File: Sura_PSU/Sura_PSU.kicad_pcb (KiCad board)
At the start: 2 copper layers, 100 x 183 mm, 16 parts, among them J1 12VDC In, J2 X11, J3 X11, U1 PSU2-5, U2 NKE1212SC

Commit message: Initial commit (to be tested)
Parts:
- J1: value 12VDC In -> 12V In; footprint Connector_JST:JST_VH_B2P-VH_1x02_P3.96mm_Vertical -> Clueless_Engineer:694106301002
- moved H4 179.3 mm to (58.1, 47.7)
- moved H3 137.3 mm to (133.1, 47.7)
- moved J1 128.4 mm to (52.1, 181.7)
- moved F1 116.9 mm to (76.2, 181.7), turned to 90 degrees
- moved C1 81.8 mm to (124.4, 165.7)
- moved C2 81.8 mm to (115.5, 165.7)
- moved U1 80.3 mm to (88.9, 161.9), turned to -90 degrees
- moved C4 6.40 mm to (115.5, 112.3), turned to 90 degrees
- moved C3 6.39 mm to (106.8, 112.3), turned to 90 degrees
- moved H1 1.00 mm to (133.1, 220.7)
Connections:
- F1 pad 1: Net-(J1-Pin_2) -> Net-(F1-Pad1)
- J1 pad 1: /GND -> Net-(F1-Pad1)
- J1 pad 2: Net-(J1-Pin_2) -> /GND
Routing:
- net /GND: track 346.1 -> 285.7 mm
- net Net-(F1-Pad1): track 0.00 -> 29.1 mm
- net Net-(J1-Pin_2): track 18.5 -> 0.00 mm
- net /+12V: track 212.9 -> 224.3 mm
- net /+5V: track 152.8 -> 157.4 mm
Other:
- board text added: "Brett Hallen May 2026"
- board text added: "Regulated +12VDC Input"
- board text removed: "Brett Hallen, May 2026"
- board text removed: "WORK IN PROGRESS"

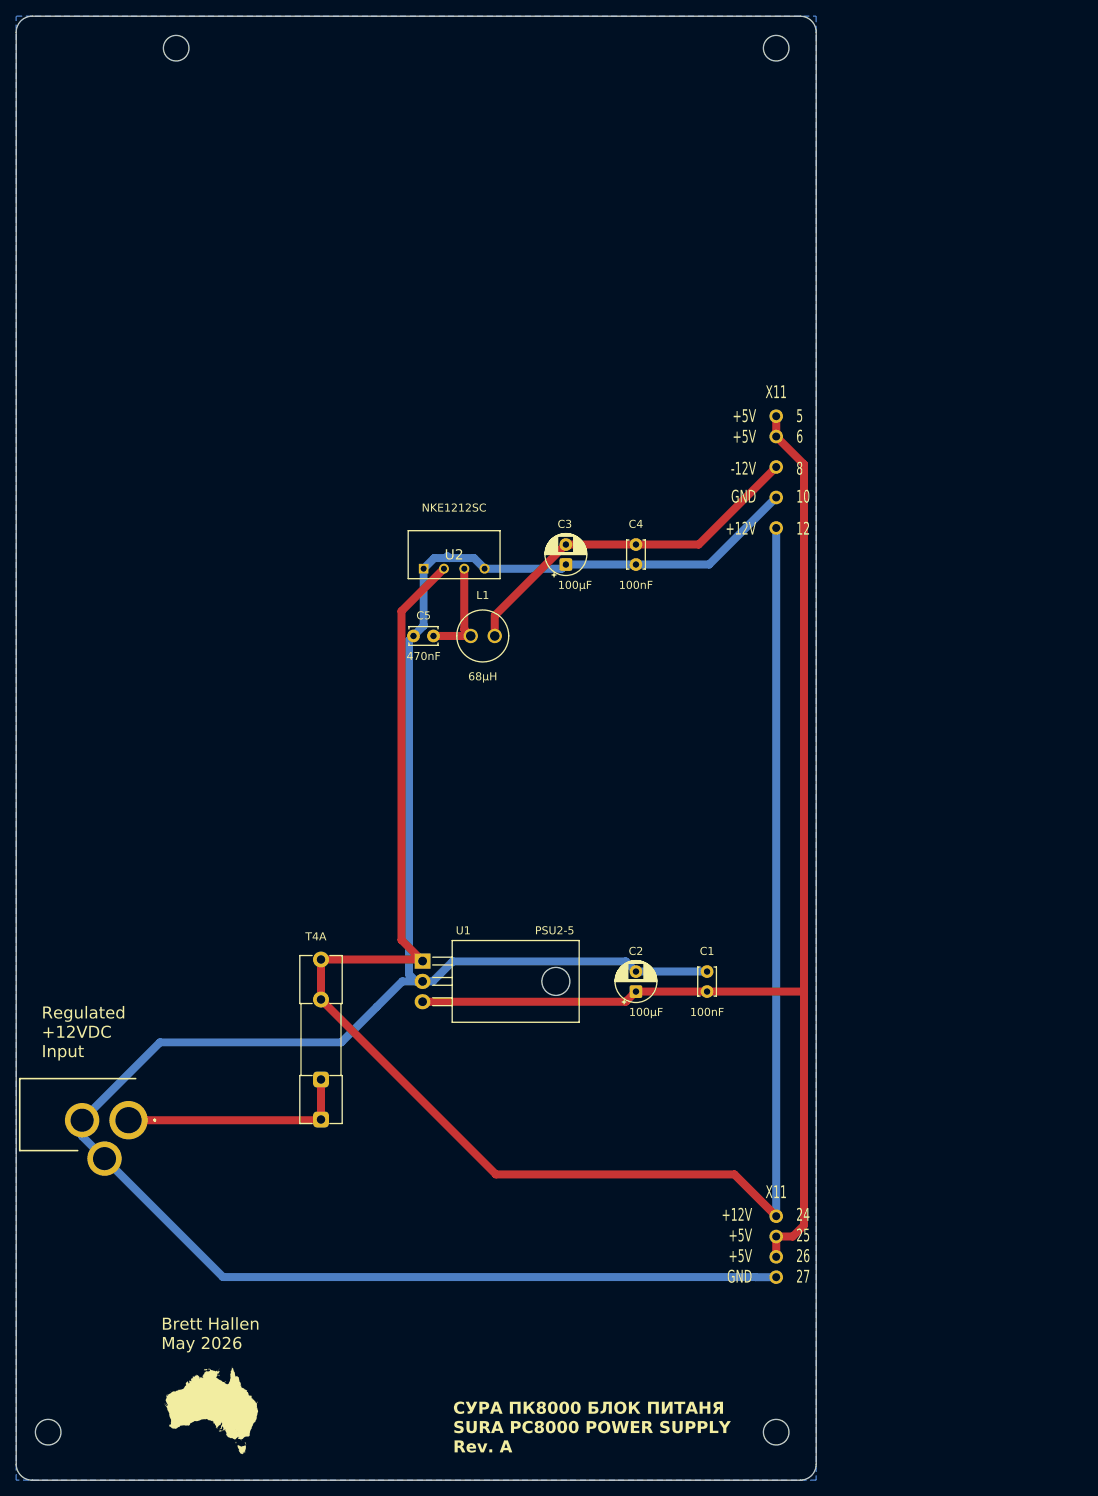
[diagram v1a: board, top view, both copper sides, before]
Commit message: Updated design (swapped 5V regulator)
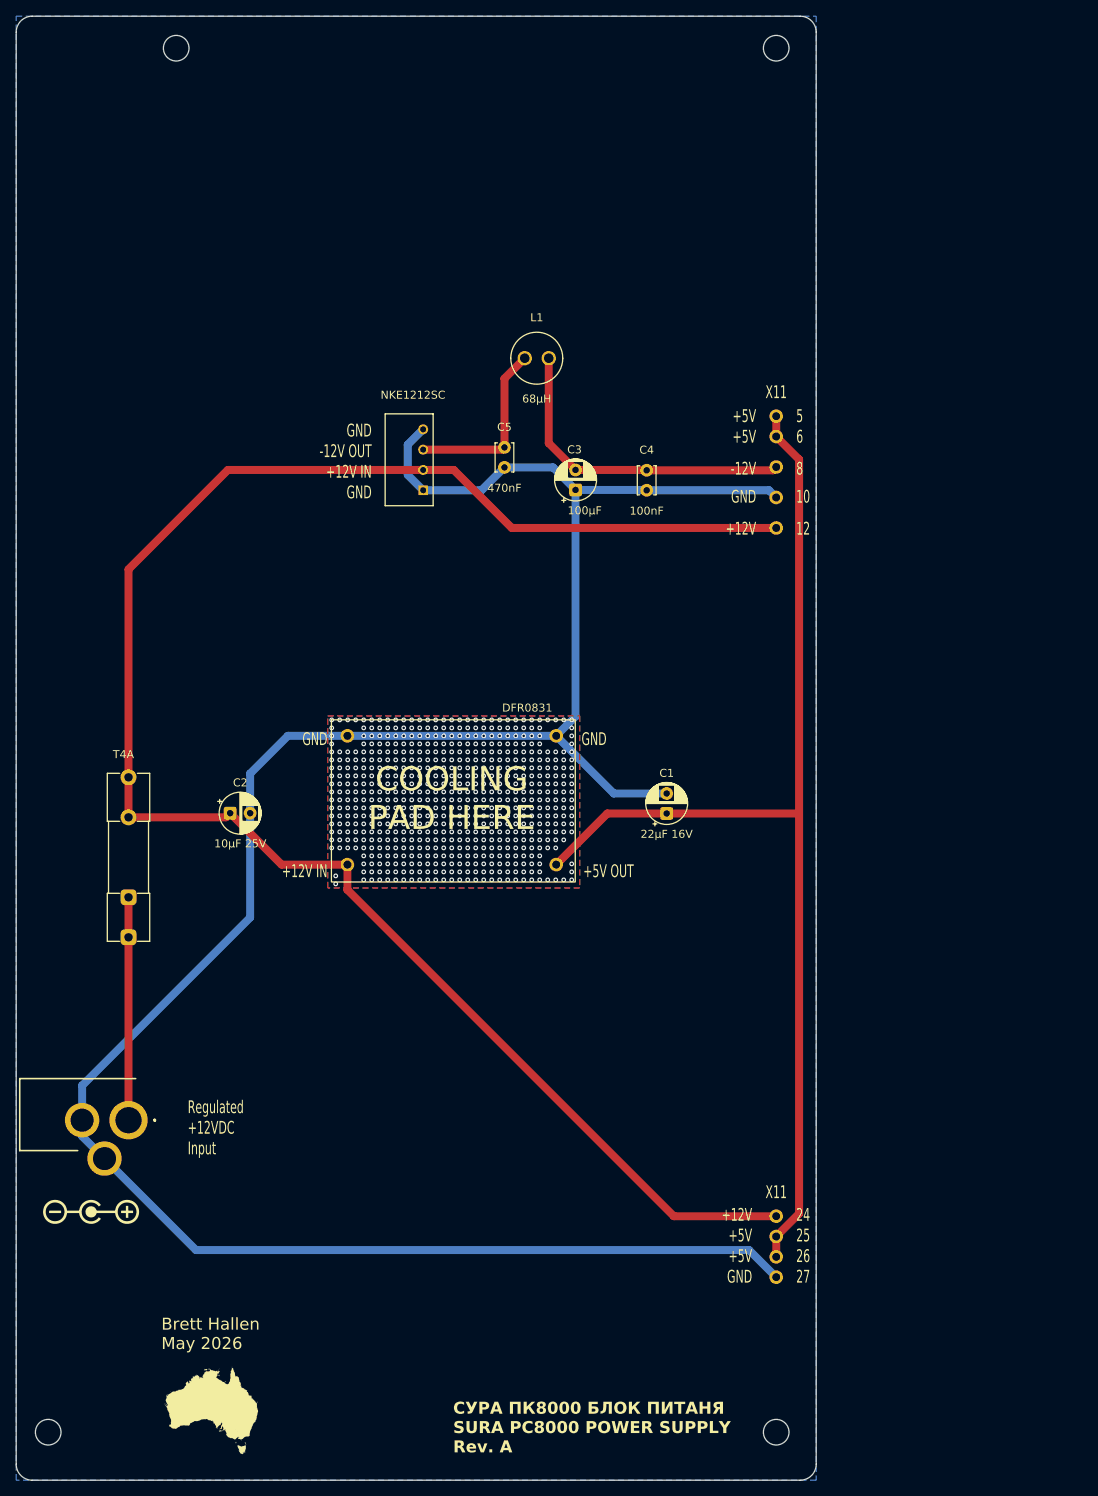
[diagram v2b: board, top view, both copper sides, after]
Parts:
- C1: value 100nF -> 22µF 16V; footprint Capacitor_THT:C_Disc_D3.4mm_W2.1mm_P2.50mm -> Capacitor_THT:CP_Radial_D5.0mm_P2.50mm
- C2: value 100µF -> 10µF 25V
- U1: value PSU2-5 -> DFR0831; footprint Package_TO_SOT_THT:TO-220-3_Horizontal_TabDown -> Clueless_Engineer:DFR0831
- moved C2 55.4 mm to (64.8, 143.4), turned to 0 degrees
- moved L1 35.4 mm to (101.6, 86.5)
- moved F1 33.1 mm to (52.1, 158.9)
- moved U1 32.0 mm to (90.9, 130.0), turned to 0 degrees
- moved C5 25.2 mm to (99.1, 97.6), turned to -90 degrees
- moved C1 22.8 mm to (119.4, 143.4)
- moved U2 9.80 mm to (88.9, 103.0), turned to 90 degrees
- moved C3 9.40 mm to (108.0, 103.0)
- moved C4 9.38 mm to (116.9, 103.0)
- renumbered J2 to J1, J1 to J2
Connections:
- C2 pad 1: /+5V -> /+12V
- U1 pad 1: /+12V -> /GND
- U1 pad 2: /GND -> /+12V
- U1 pad 3: /+5V -> /GND
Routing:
- net /+5V: track 157.4 -> 140.5 mm
- net Net-(U2--VOUT): track 13.4 -> 22.5 mm
- net /GND: track 285.7 -> 292.9 mm, vias 0 -> 606
- net /-12V: track 45.4 -> 40.6 mm
- net Net-(F1-Pad1): track 29.1 -> 27.9 mm
- added copper zone on F.Cu, net /GND
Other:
- board text added: "COOLING PAD HERE"
- board text added: "GND -12V OUT +12V IN GND"
